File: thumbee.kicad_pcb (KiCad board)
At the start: 2 copper layers, 38 x 38 mm, 60 parts, among them J11 Conn_02x05_Odd_Even, J12 USB_B, U1 msc313e, U2 spinor, U3 ht42b534-1, U4 RT8059GJ5, U5 RT8059GJ5, U6 RT8059GJ5, U7 xc6204xxxxMR, Y1 Crystal

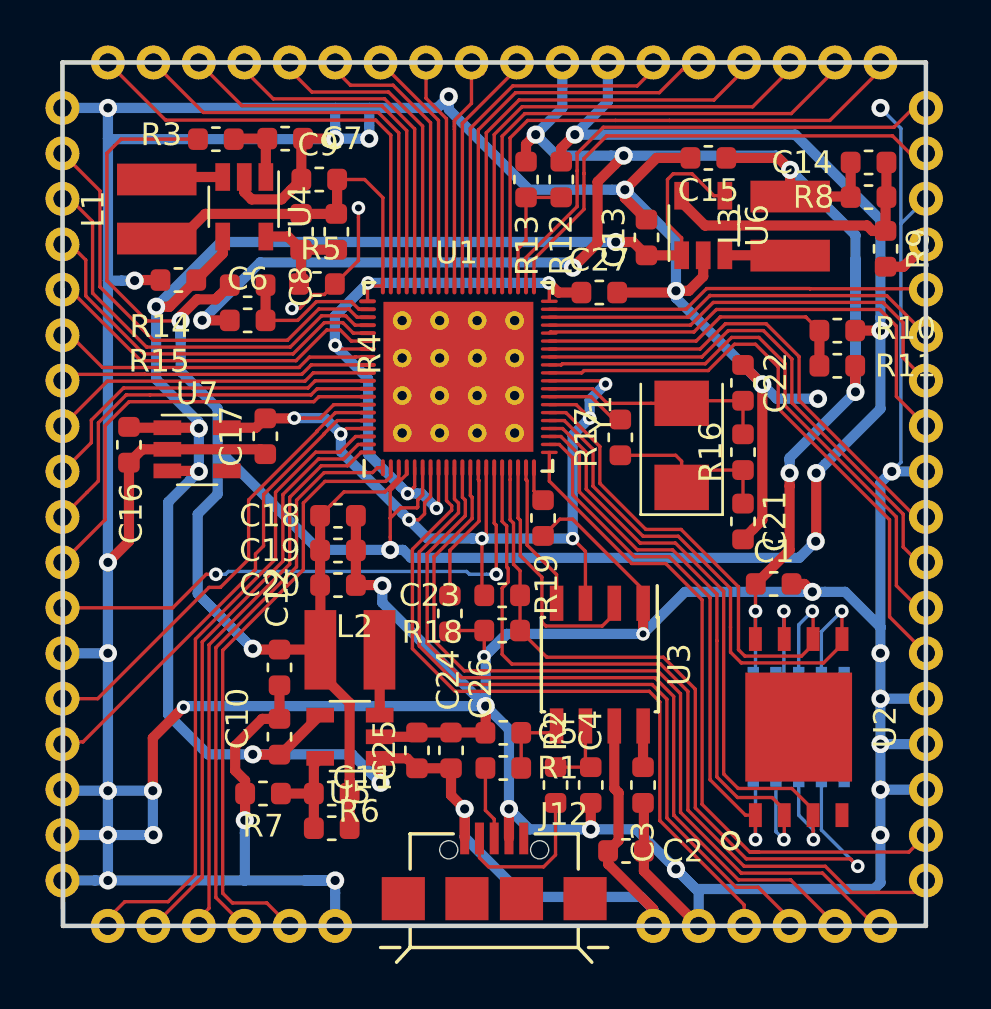
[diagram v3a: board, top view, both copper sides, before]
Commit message: Some clean up. Add some decoupling caps in the left over space.
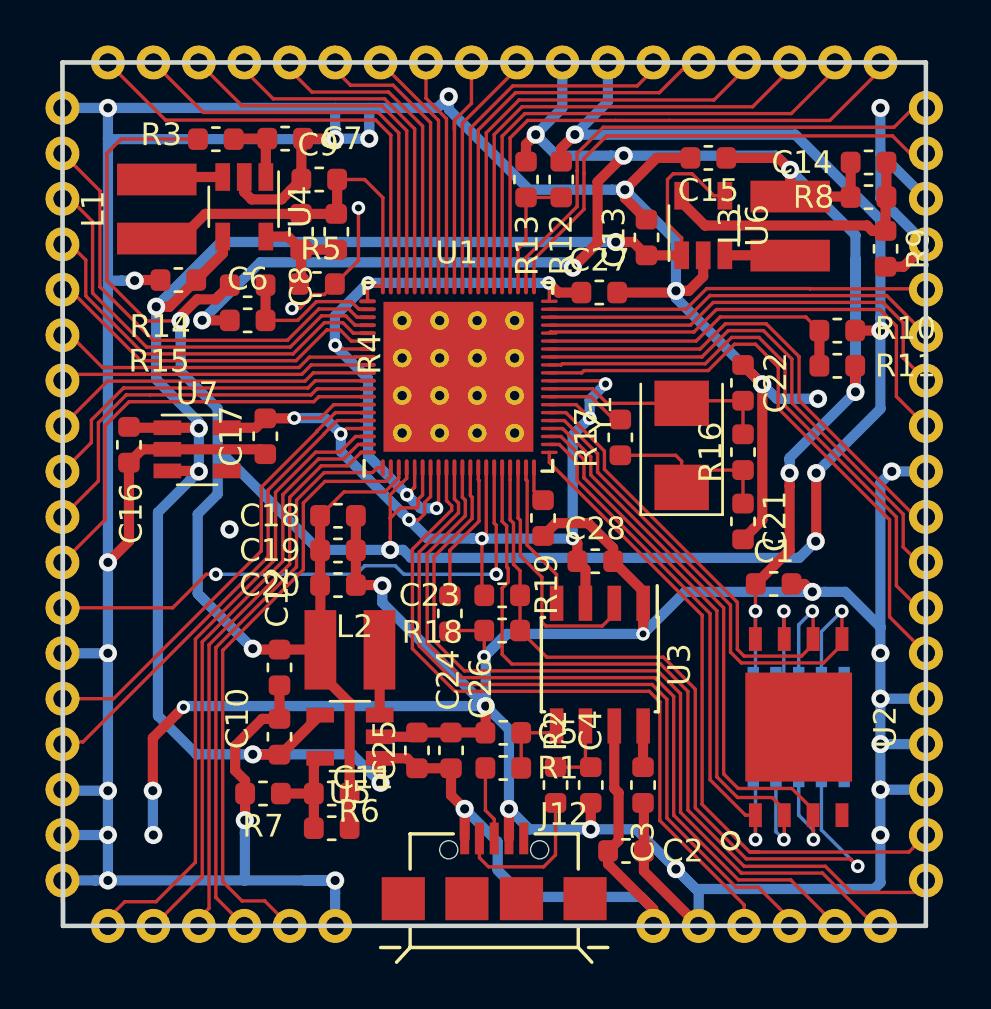
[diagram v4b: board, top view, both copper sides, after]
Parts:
- added C28: C, Capacitor_SMD:C_0603_1608Metric, F.Cu at (158.5, 101.1)
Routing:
- net GND: track 315.8 -> 302.2 mm, vias 36 -> 37
- net /spinor_mosi: track 25.5 -> 24.6 mm
- net /spinor_wp: track 29.1 -> 28.2 mm
- net /spinor_miso: track 27.6 -> 26.7 mm
- net /spinor_cs: track 25.9 -> 25.0 mm
- net /spinor_sck: track 24.0 -> 23.1 mm
- net /pm_gpio4: track 30.1 -> 29.2 mm
- net +5V: track 102.6 -> 103.2 mm

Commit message: Rev0
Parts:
- added C29: C, Capacitor_SMD:C_0603_1608Metric, F.Cu at (167.9, 98.7)
- added C30: C, Capacitor_SMD:C_0603_1608Metric, F.Cu at (167.9, 100.3)
- added C31: C, Capacitor_SMD:C_0603_1608Metric, F.Cu at (140.3, 98.7)
- added C32: C, Capacitor_SMD:C_0603_1608Metric, F.Cu at (140.4, 100.4)
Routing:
- net +1V8: track 131.3 -> 142.2 mm, vias 7 -> 8
- net GND: track 302.2 -> 310.5 mm, vias 37 -> 36
- net /eth_tp: track 21.4 -> 22.4 mm
- net /eth_tn: track 22.9 -> 23.9 mm
- net /eth_rp: track 24.5 -> 25.5 mm
- net /eth_rn: track 25.8 -> 26.8 mm
- net /spinor_mosi: track 24.6 -> 24.1 mm
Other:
- board text added: "thumbee rev0 ~dgp"

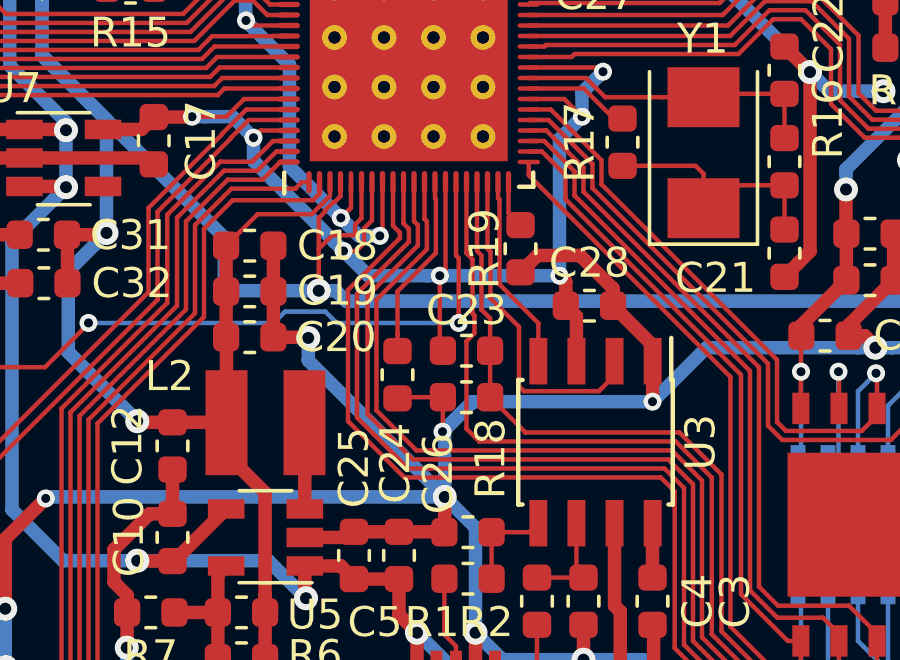
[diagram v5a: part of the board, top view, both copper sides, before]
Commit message: Re-route avdd_nodie and dvdd_nodie
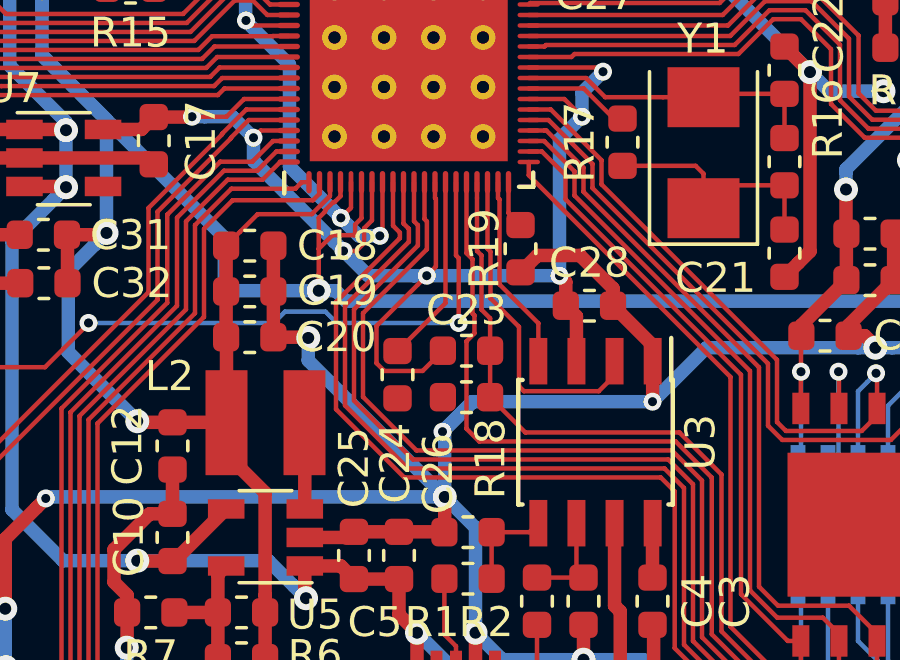
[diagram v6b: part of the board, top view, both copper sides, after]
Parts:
- C10, C13, C6: value C -> 4.7uf
- C11, C14, C8: value C -> 22pf
- C12, C15, C16, C2, C9: value C -> 10uf
- C17, C3: value C -> 1uf
- C23: value C -> 2.2uf
- C4, C5: value C -> 47pf
- C7: value C -> 470nf
- R1, R2: value R -> 33
- R18, R5: value R -> 100k
- R3: value R -> 10k
- R4: value R -> 75k
- R6: value R -> 120k
- R7: value R -> 57k
- R8: value R -> 33k
- R9: value R -> 7.5k
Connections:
- U1 pad 13: /dvdd_nodie -> +3.3VA
- U1 pad 14: +3.3VA -> /dvdd_nodie
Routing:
- net +3.3VA: track 46.8 -> 50.4 mm
- net GND: track 310.5 -> 307.9 mm

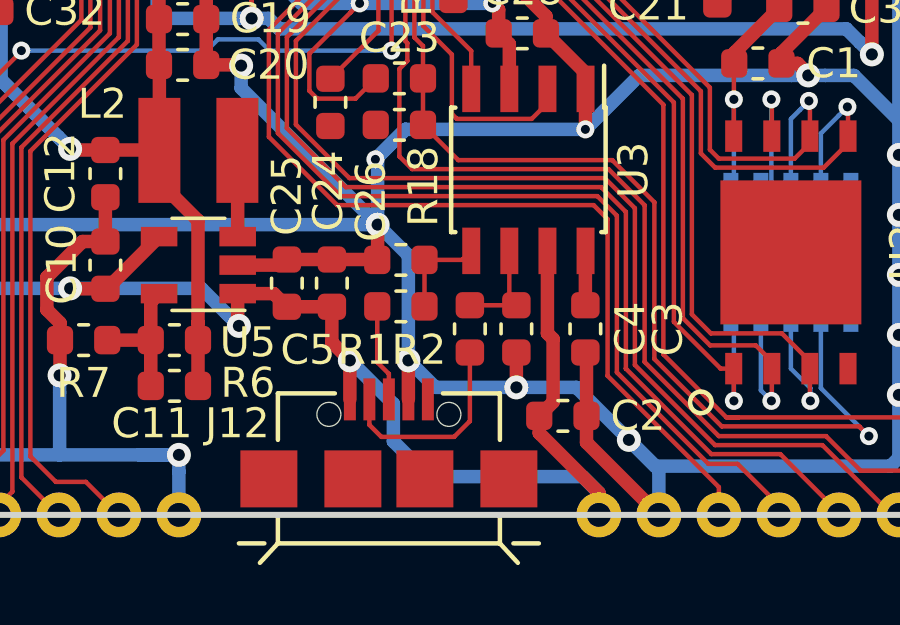
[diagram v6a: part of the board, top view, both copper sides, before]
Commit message: Fix USB pinout
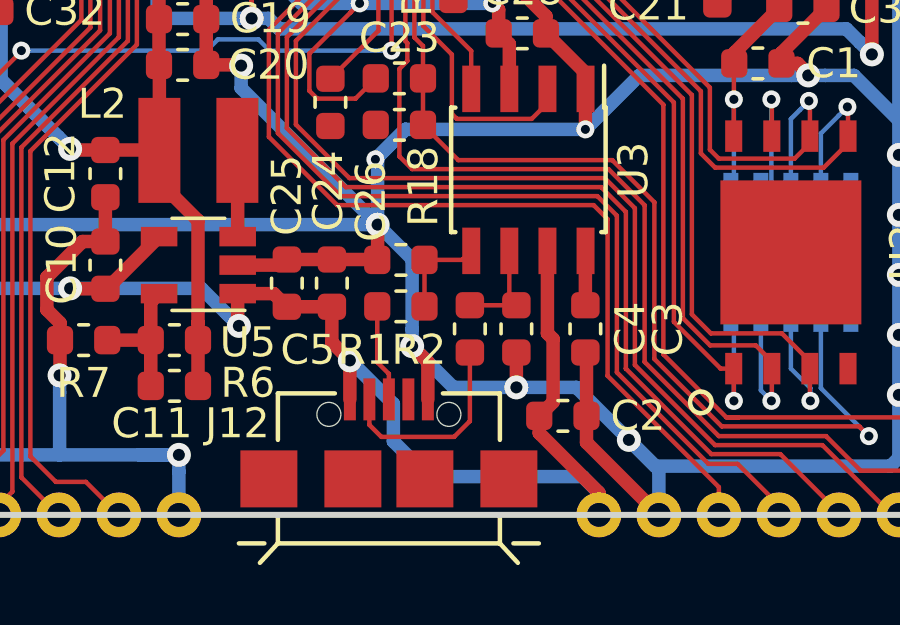
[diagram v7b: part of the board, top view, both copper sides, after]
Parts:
- J12: value USB_B -> USB_B_Mini
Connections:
- J12 pad 4: GND -> Net-(J12-Pad4)
- J12 pad 5: Net-(J12-Pad5) -> GND
- J12 pad 6: (no net) -> Net-(J12-Pad6)
